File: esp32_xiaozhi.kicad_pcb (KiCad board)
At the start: 2 copper layers, 99.1 x 99.1 mm, 139 parts, among them J1 FT232RL, J10 Micro_SD_Card, J3 USB_B_Mini, J5 Oled SSD1306 128x32, J7 Conn_01x07_Pin, J9 Adafruit ST7789, Q10 FDN306P, Q11 FDN306P, Q2 2N7002, Q4 Q_NPN_BCE, Q5 Q_NPN_BCE, Q6 2N7002, Q7 Q_NPN_BCE, Q8 Q_NPN_BCE, Q9 2N7002, SW1 SW_Push, SW10 rigth, SW2 SW_Push, SW3 up, SW4 down, SW5 left, SW6 rigth, SW7 up, SW8 down, SW9 left, U1 ESP32-C6-WROOM-1-N8, U2 ESP32-C6-DEVKITC-1-N8, U3 FT232BM, U4 LM1117DT-3.3, U5 MAX98357A, U6 ER_OLEDM0.91_1x-I2C, U7 TXS0108EPW, Y1 Crystal

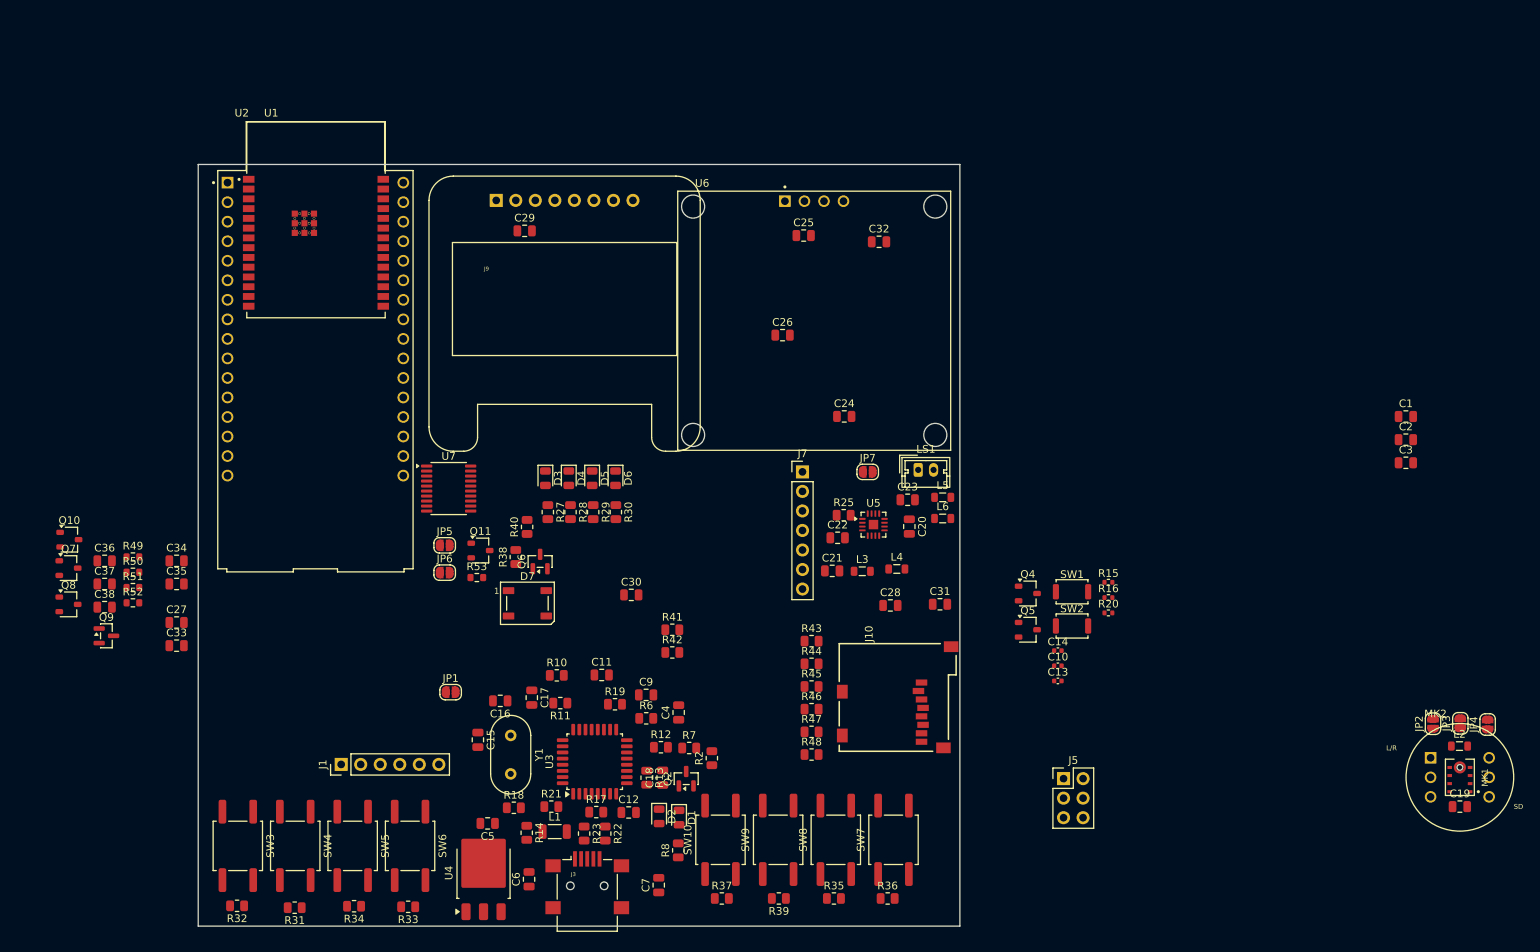
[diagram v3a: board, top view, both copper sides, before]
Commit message: Update all footprint reference fonts to match Q13 (Arial, 0.7x0.7, 0.1 thickness)
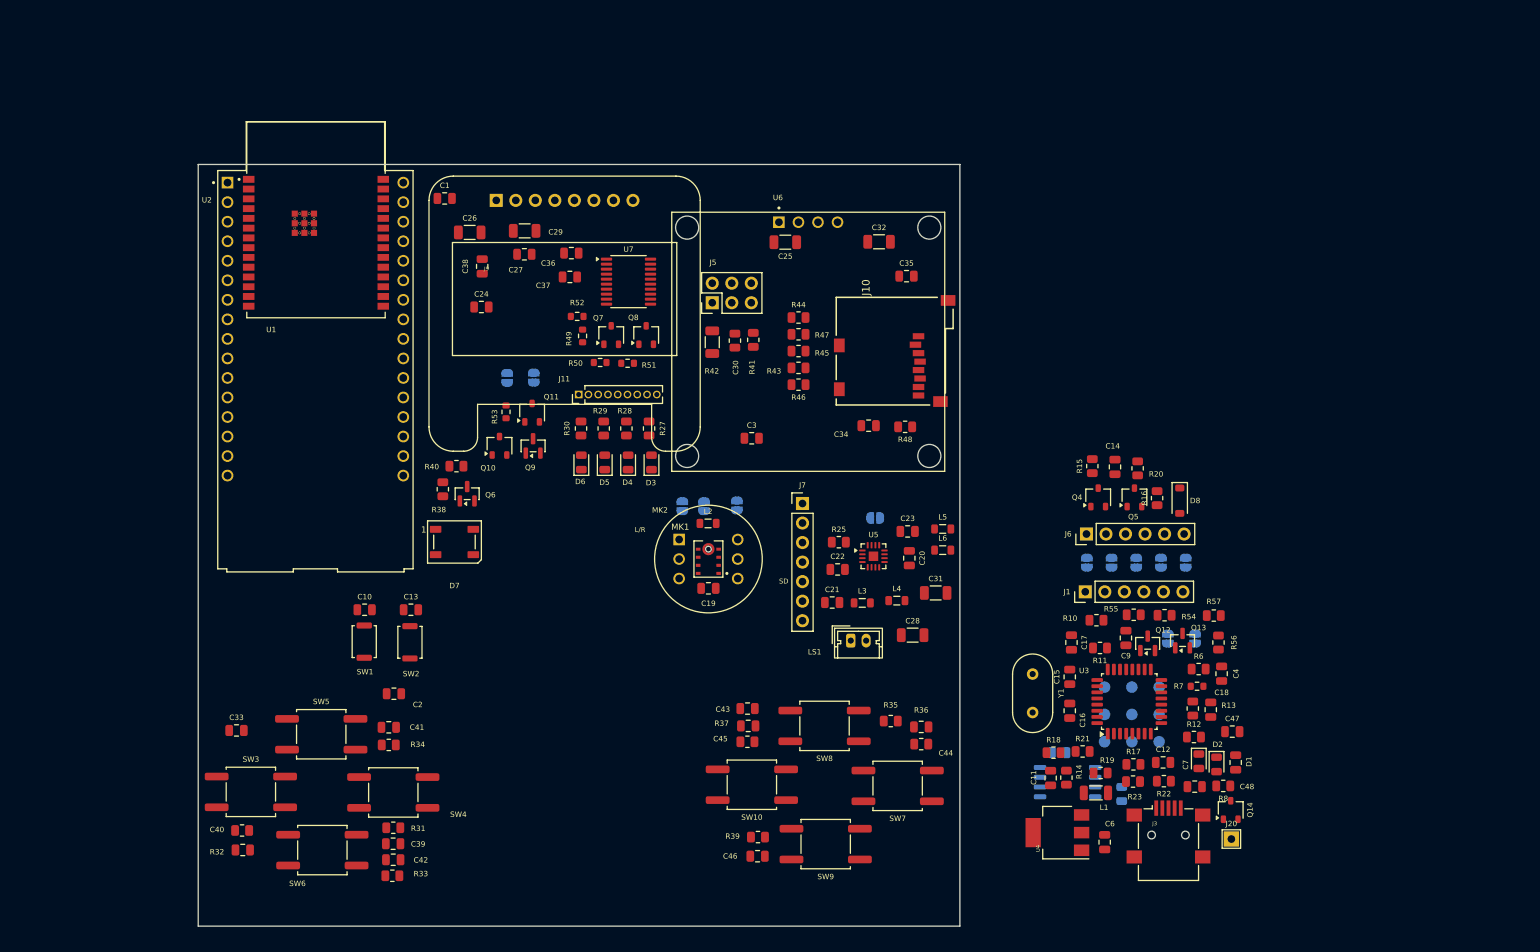
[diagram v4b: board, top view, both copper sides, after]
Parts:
- removed JP1: Jumper_2_Open, Jumper:SolderJumper-2_P1.3mm_Open_RoundedPad1.0x1.5mm
- removed Q2: 2N7002, Package_TO_SOT_SMD:SOT-23
- removed R2: 10K, Resistor_SMD:R_0805_2012Metric
- added C39: 100nf, Capacitor_SMD:C_0805_2012Metric, F.Cu at (81.2, 141.7)
- added C40: 100nf, Capacitor_SMD:C_0805_2012Metric, F.Cu at (61.7, 142.5)
- added C41: 100nf, Capacitor_SMD:C_0805_2012Metric, F.Cu at (80.7, 126.5)
- added C42: 100nf, Capacitor_SMD:C_0805_2012Metric, F.Cu at (81.2, 143.8)
- added C43: 100nf, Capacitor_SMD:C_0805_2012Metric, F.Cu at (127.3, 124.1)
- added C44: 100nf, Capacitor_SMD:C_0805_2012Metric, F.Cu at (149.9, 126.5)
- added C45: 100nf, Capacitor_SMD:C_0805_2012Metric, F.Cu at (127.4, 126.4)
- added C46: 100nf, Capacitor_SMD:C_0805_2012Metric, F.Cu at (128.6, 143.3)
- added C47: 100nf, Capacitor_SMD:C_0805_2012Metric, F.Cu at (190.4, 127.1)
- added C48: 100nf, Capacitor_SMD:C_0805_2012Metric, F.Cu at (190.8, 131.1)
- added D8: 1N4148W, Diode_SMD:D_SOD-123, F.Cu at (183.5, 97.1)
- added J11: logic_convert, Connector_PinHeader_1.27mm:PinHeader_1x09_P1.27mm_Vertical, F.Cu at (105.4, 83.3)
- added J12: tp, TestPoint:TestPoint_Pad_D1.5mm, B.Cu at (180.9, 124.9)
- added J13: tp, TestPoint:TestPoint_Pad_D1.5mm, B.Cu at (180.9, 128.4)
- added J14: tp, TestPoint:TestPoint_Pad_D1.5mm, B.Cu at (177.3, 121.3)
- added J15: tp, TestPoint:TestPoint_Pad_D1.5mm, B.Cu at (177.3, 124.9)
- added J16: tp, TestPoint:TestPoint_Pad_D1.5mm, B.Cu at (177.3, 128.4)
- added J17: tp, TestPoint:TestPoint_Pad_D1.5mm, B.Cu at (173.8, 121.3)
- added J18: tp, TestPoint:TestPoint_Pad_D1.5mm, B.Cu at (173.8, 124.9)
- added J19: tp, TestPoint:TestPoint_Pad_D1.5mm, B.Cu at (173.8, 128.4)
- added J20: tp, TestPoint:TestPoint_THTPad_2.0x2.0mm_Drill1.0mm, F.Cu at (190.2, 141.1)
- added J6: FT232RL, Connector_PinHeader_2.54mm:PinHeader_1x06_P2.54mm_Vertical, F.Cu at (171.4, 101.4)
- added J8: tp, TestPoint:TestPoint_Pad_D1.5mm, B.Cu at (180.9, 121.3)
- added JP10: Jumper_Open, Jumper:SolderJumper-2_P1.3mm_Open_RoundedPad1.0x1.5mm, B.Cu at (181.1, 105.1)
- added JP11: Jumper_Open, Jumper:SolderJumper-2_P1.3mm_Open_RoundedPad1.0x1.5mm, B.Cu at (171.4, 105.1)
- added JP12: Jumper_Open, Jumper:SolderJumper-2_P1.3mm_Open_RoundedPad1.0x1.5mm, B.Cu at (177.9, 105.1)
- added JP13: Jumper_Open, Jumper:SolderJumper-2_P1.3mm_Open_RoundedPad1.0x1.5mm, B.Cu at (174.7, 105.1)
- added JP14: Jumper_Open, Jumper:SolderJumper-2_P1.3mm_Open_RoundedPad1.0x1.5mm, B.Cu at (184.3, 105.1)
- added JP15: Jumper_Open, Jumper:SolderJumper-2_P1.3mm_Open_RoundedPad1.0x1.5mm, B.Cu at (182.0, 115.0)
- added JP16: Jumper_Open, Jumper:SolderJumper-2_P1.3mm_Open_RoundedPad1.0x1.5mm, B.Cu at (185.5, 115.0)
- added Q12: 2N7002, Package_TO_SOT_SMD:SOT-23, F.Cu at (179.4, 115.6)
- added Q13: 2N7002, Package_TO_SOT_SMD:SOT-23, F.Cu at (183.9, 115.3)
- added Q14: FDN306P, Package_TO_SOT_SMD:SOT-23W, F.Cu at (190.2, 137.3)
- added R24: 2k2, Resistor_SMD:R_0805_2012Metric, B.Cu at (176.0, 135.2)
- added R54: 2k2, Resistor_SMD:R_0805_2012Metric, F.Cu at (181.6, 112.0)
- added R55: 2k2, Resistor_SMD:R_0805_2012Metric, F.Cu at (177.5, 111.9)
- added R56: 2k2, Resistor_SMD:R_0805_2012Metric, F.Cu at (188.6, 115.5)
- added R57: 2k2, Resistor_SMD:R_0805_2012Metric, F.Cu at (188.0, 112.0)
- added U8: 93CxxA, Package_SO:SOIC-8_5.3x5.3mm_P1.27mm, B.Cu at (169.0, 133.7)
- C10, C13, C14: footprint Capacitor_SMD:C_0402_1005Metric -> Capacitor_SMD:C_0805_2012Metric
- C25, C26, C28, C29, C30, C31, C32: footprint Capacitor_SMD:C_0805_2012Metric -> Capacitor_SMD:C_1206_3216Metric
- C5, JP2, JP5, JP6, JP7: moved to B.Cu
- J7: value Conn_01x07_Pin -> ~
- JP3, JP4: value Jumper_2_Open -> Jumper_Open; moved to B.Cu
- R15, R16, R20: footprint Resistor_SMD:R_0402_1005Metric -> Resistor_SMD:R_0805_2012Metric
- R7: footprint Resistor_SMD:R_0805_2012Metric -> Resistor_SMD:R_0603_1608Metric
- U4: footprint Package_TO_SOT_SMD:TO-252-3_TabPin2 -> kiC:SOT-223-3_TabPin2
- moved C2 135.7 mm to (81.3, 122.2)
- moved C1 128.2 mm to (87.9, 57.8)
- moved JP4 108.5 mm to (118.8, 97.8)
- moved C35 103.0 mm to (148.0, 67.9)
- moved JP3 102.3 mm to (121.7, 97.8)
- moved L2 101.9 mm to (122.2, 100.0)
- moved C19 101.8 mm to (122.2, 108.5)
- moved MK1 101.8 mm to (122.2, 104.7)
- moved MK2 101.8 mm to (122.2, 104.7)
- moved J1 99.3 mm to (171.2, 108.9)
- moved JP2 94.9 mm to (125.9, 97.7), turned to -90 degrees
- moved SW1 92.3 mm to (77.5, 115.4), turned to 90 degrees
- moved C34 91.7 mm to (143.1, 87.3)
- moved C10 90.5 mm to (77.5, 111.3)
- moved SW2 86.1 mm to (83.4, 115.5), turned to 90 degrees
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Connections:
- net /esp32_C6/IO_16 renamed /MTX
- net /esp32_C6/IO_17 renamed /MRX
- net /ft232/FT renamed /ft232/FT_CTL
- net /ft232/V+_USB renamed +5VA
- C10 pad 1: /ft232/EN -> /EN
- C11 pad 2: GND -> GND1
- C12 pad 2: GND -> GND1
- C13 pad 1: /ft232/GPIO0 -> /esp32_C6/GPIO0
- C14 pad 1: /ft232/EN -> /EN
- C18 pad 2: +3V3 -> +3.3VA
- C4 pad 1: +3V3 -> +3.3VA
- C4 pad 2: GND -> GND1
- C5 pad 1: +3V3 -> +3.3VA
- C5 pad 2: GND -> GND1
- C6 pad 1: GND -> GND1
- C6 pad 2: +3V3 -> +3.3VA
- C7 pad 1: GND -> GND1
- C7 pad 2: +3V3 -> +3.3VA
- Q4 pad 2: /ft232/EN -> /EN
- Q4 pad 3: /ft232/FT_RST -> /CTS
- Q5 pad 2: /ft232/GPIO0 -> /esp32_C6/IO_0
- Q5 pad 3: /ft232/FT_DTR -> /DTR
- R12 pad 1: +3V3 -> +3.3VA
- R13 pad 1: +3V3 -> +3.3VA
- R15 pad 1: /ft232/FT_DTR -> /DTR
- R16 pad 1: /ft232/FT_RST -> /CTS
- R18 pad 1: +3V3 -> +3.3VA
- R20 pad 2: /ft232/EN -> /EN
- R7 pad 2: Net-(Q2-G) -> /ft232/pwr_en
- R8 pad 1: +3V3 -> +3.3VA
- SW1 pad 2: /ft232/EN -> /EN
- SW2 pad 2: /ft232/GPIO0 -> /esp32_C6/GPIO0
- U1 pad 3: /esp32_C6/EN -> /EN
- U2 pad J1_2: /esp32_C6/EN -> /EN
- U3 pad 13: +3V3 -> +3.3VA
- U4 pad 2: +3V3 -> +3.3VA
